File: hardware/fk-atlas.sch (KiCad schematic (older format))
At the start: 50 parts, among them J1 CONN-HDR-2x5, J2 MICRO-USB, J3 Conn_01x02, J4 Conn_01x07, Q1 2N7002LT1G, Q2 2N7002LT1G, Q3 2N7002LT1G, Q4 2N7002LT1G, Q5 2N7002LT1G, SW1 SPNO, U1 S25FL1xxK0XM, U2 ATSAMD21G18A-AU, U3 MCP1700T-3302E/MB, Y1 FC-135

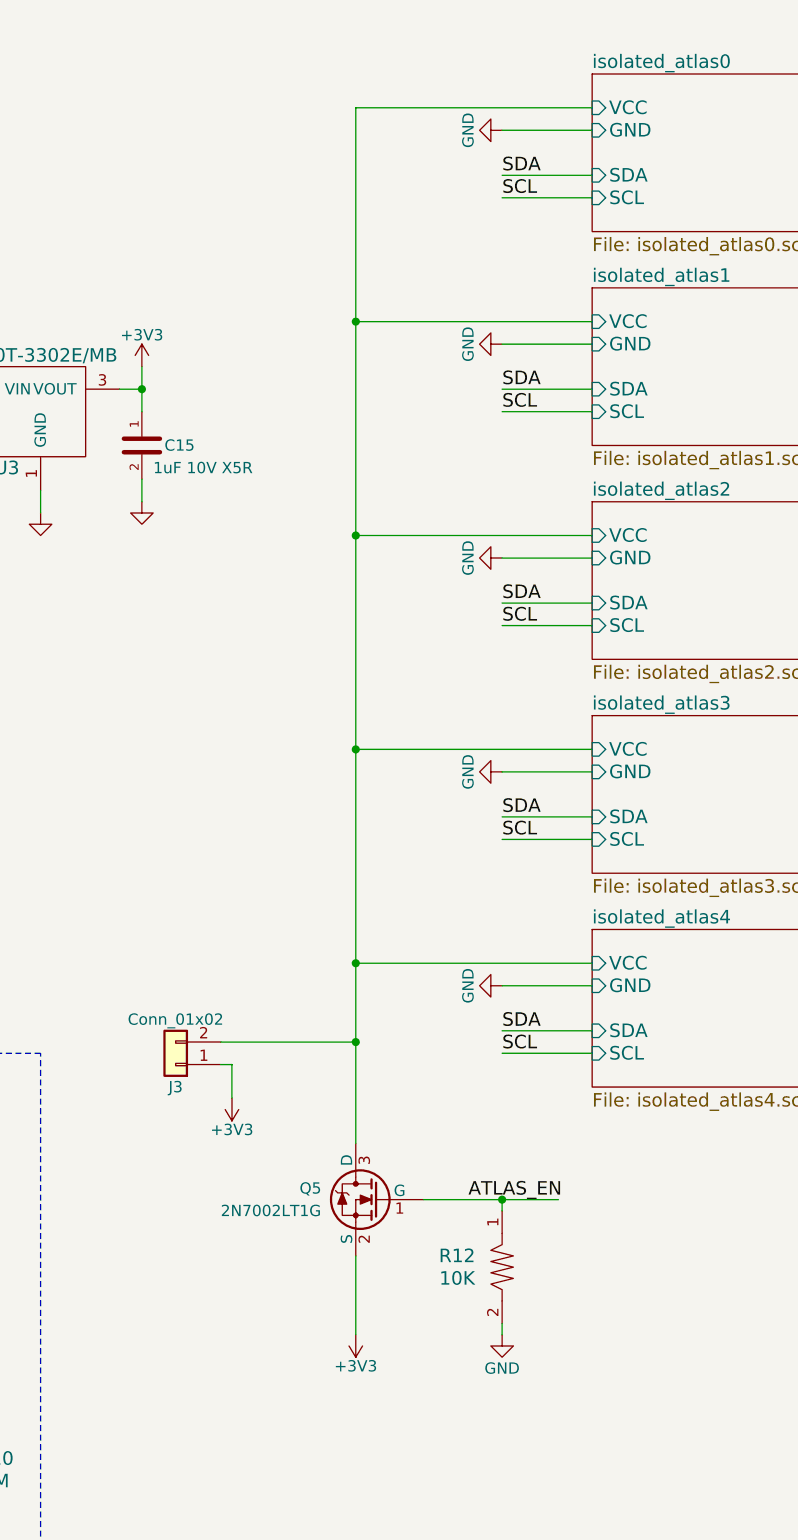
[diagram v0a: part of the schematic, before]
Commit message: Convert atlas enable to low side switch.
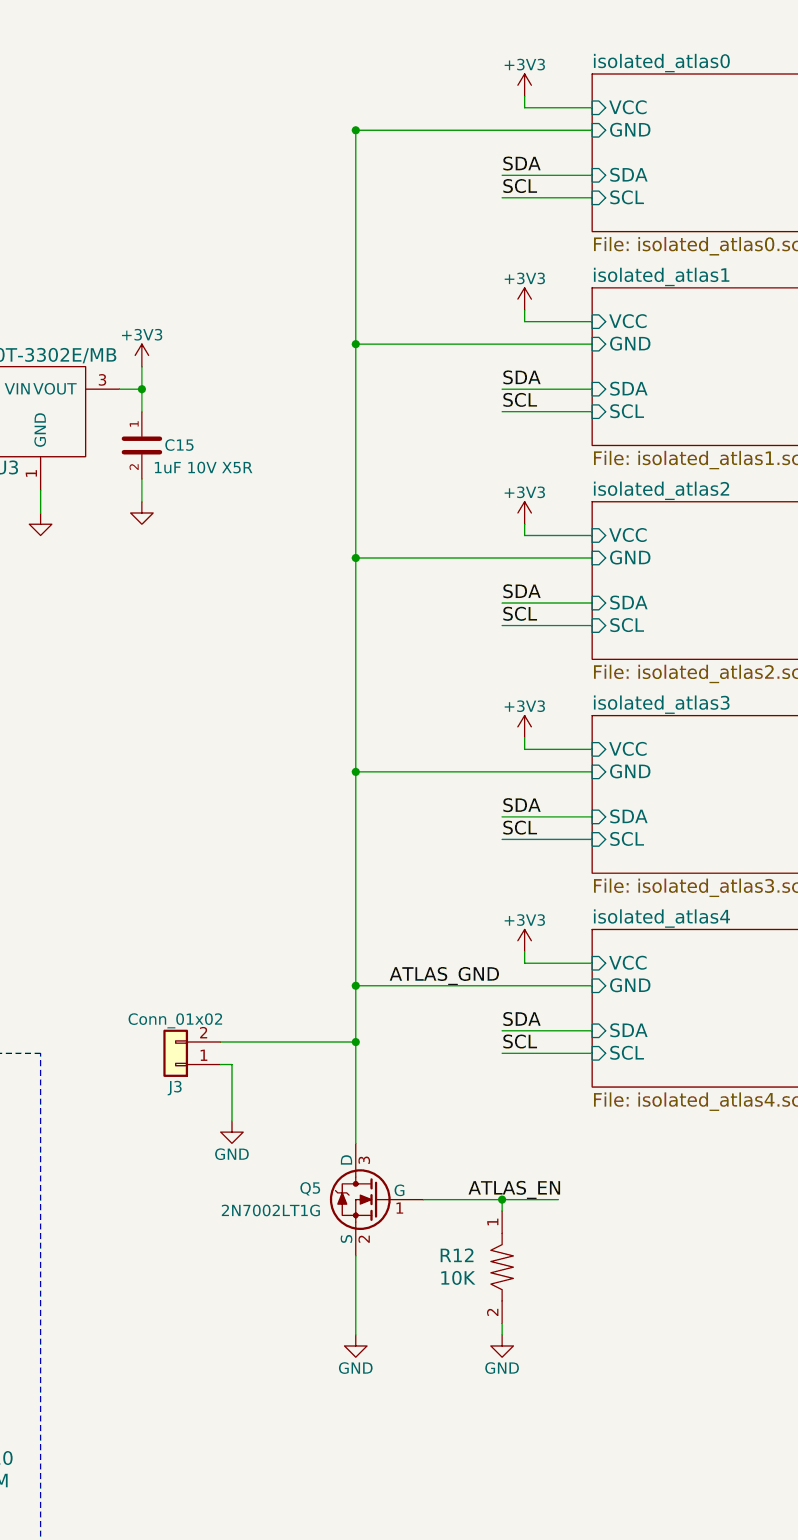
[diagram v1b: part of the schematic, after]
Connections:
- net labels added: ATLAS_GND
- wire segments 211 -> 216

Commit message: Break out Wire3 instead of Wire2.
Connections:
- net labels added: FLASH_CS, SCL1, SCL3, SDA1, SDA3
- net labels removed: D12, D3, D4, D5, SCL, SCL2, SDA, SDA2
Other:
- note removed: "RX1"
- note removed: "TX1"
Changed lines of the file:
@@
 	0    -1   -1   0
 $EndComp
-Text Label 2500 6800 0    60   ~ 0
-SCL
-Text Label 2500 6900 0    60   ~ 0
-SDA
-Text Label 4050 6050 0    60   ~ 0
-SDA
-Text Label 4050 5950 0    60   ~ 0
-SCL
+Text Label 2800 6800 0    50   ~ 0
+SCL1
+Text Label 2800 6900 0    50   ~ 0
+SDA1
+Text Label 4050 6050 0    50   ~ 0
+SDA1
+Text Label 4050 5950 0    50   ~ 0
+SCL1
 Text Label 13750 1400 0    60   ~ 0
-SCL
+SCL1
 Text Label 13750 1300 0    60   ~ 0
-SDA
+SDA1
 Text Label 13750 2350 0    60   ~ 0
-SCL
+SCL1
 Text Label 13750 2250 0    60   ~ 0
-SDA
+SDA1
 Text Label 13750 3300 0    60   ~ 0
-SCL
+SCL1
 Text Label 13750 3200 0    60   ~ 0
-SDA
+SDA1
 Text Label 13750 4250 0    60   ~ 0
-SCL
+SCL1
 Text Label 13750 4150 0    60   ~ 0
-SDA
+SDA1
 Text Label 13750 5200 0    60   ~ 0
-SCL
+SCL1
 Text Label 13750 5100 0    60   ~ 0
-SDA
+SDA1
 Text Label 2550 2300 0    50   ~ 0
 A0
@@
 Text Label 2550 2800 0    50   ~ 0
 D9
-Text Label 2550 2900 0    50   ~ 0
-D4
-Text Label 2550 3000 0    50   ~ 0
-D3
 Text Label 2550 3100 0    50   ~ 0
 D1
@@
 Text Label 2550 3500 0    50   ~ 0
 D2
-Text Label 2550 3600 0    50   ~ 0
-D5
 Text Label 2550 3700 0    50   ~ 0
 D11
 Text Label 2550 3900 0    50   ~ 0
 D10
-Text Label 2550 4000 0    50   ~ 0
-D12
 Text Label 2550 4100 0    50   ~ 0
 D6
@@
 D7
 Text Label 2550 4300 0    50   ~ 0
-SDA
+SDA1
 Text Label 2550 4400 0    50   ~ 0
-SCL
+SCL1
 Text Label 4550 3000 0    50   ~ 0
 MOSI
@@
 Text Notes 4850 2800 0    50   ~ 0
 RX0
-Text Notes 2350 3200 0    50   ~ 0
-RX1
-Text Notes 2350 3100 0    50   ~ 0
-TX1
 Text Notes 6000 4900 0    60   ~ 0
 1.27 mm (0.05")
@@
 D13
 Wire Wire Line
-	2400 6800 3200 6800
-Wire Wire Line
-	2400 6900 3500 6900
+	2800 6800 3200 6800
+Wire Wire Line
+	2800 6900 3500 6900
 Wire Wire Line
 	4350 5650 4100 5650
@@
 	2550 2800 2850 2800
 Wire Wire Line
-	2850 2900 2550 2900
-Wire Wire Line
-	2850 3000 2550 3000
+	2550 2900 2850 2900
+Wire Wire Line
+	2550 3000 2850 3000
 Wire Wire Line
 	2850 3100 2550 3100
@@
 	2850 3500 2550 3500
 Wire Wire Line
-	2850 3600 2550 3600
-Wire Wire Line
-	2000 3700 2850 3700
+	2400 3600 2850 3600
 Wire Wire Line
 	2550 3900 2850 3900
 Wire Wire Line
-	2000 4000 2850 4000
+	2400 4000 2850 4000
 Wire Wire Line
 	2850 4100 2550 4100
@@
 Wire Wire Line
 	11350 6650 11350 6750
-Wire Wire Line
-	2000 3800 2850 3800
 Wire Wire Line
 	5450 5900 5500 5900
@@
 Text Label 13600 5850 0    60   ~ 0
 ATLAS_EN
-Text Label 2000 4000 0    60   ~ 0
+Text Label 2400 4000 0    60   ~ 0
 ATLAS_EN
 Wire Wire Line
@@
 Wire Wire Line
 	12550 5250 12500 5250
-Text Label 2000 3700 0    50   ~ 0
-SDA2
-Text Label 2000 3800 0    50   ~ 0
-SCL2
+Text Label 2550 2900 0    50   ~ 0
+SDA3
+Text Label 2550 3000 0    50   ~ 0
+SCL3
 $Comp
 L Conn_01x07 J4
@@
 $EndComp
 Text Label 4050 6250 0    50   ~ 0
-SDA2
+SDA3
 Text Label 4050 6150 0    50   ~ 0
-SCL2
+SCL3
 Wire Wire Line
 	4050 6150 4350 6150
@@
 Text Label 3650 9650 0    60   ~ 0
 MOSI
-Text Label 2050 9450 0    60   ~ 0
+Text Label 1900 9450 0    60   ~ 0
 MISO
 $Comp
@@
 $EndComp
 Wire Wire Line
-	2050 9450 2350 9450
+	1900 9450 2350 9450
 Wire Wire Line
 	1850 9200 1850 9550
@@
 	1850 9550 2350 9550
 Wire Wire Line
-	2050 9350 2350 9350
-Text Label 2050 9350 0    50   ~ 0
-D5
+	1900 9350 2350 9350
+Text Label 1900 9350 0    50   ~ 0
+FLASH_CS
 $Comp
 L GND #PWR049
@@
 Text Label 13250 4900 0    60   ~ 0
 ATLAS_GND
+Wire Wire Line
+	2550 3700 2850 3700
+Wire Wire Line
+	2850 3800 2550 3800
+Text Label 2400 3600 0    50   ~ 0
+FLASH_CS
 $EndSCHEMATC

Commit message: Break out D30/D31 serial lines.
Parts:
- removed J4: Conn_01x07, Socket_Strips:Socket_Strip_Straight_1x07_Pitch2.54mm, symbol Conn_01x07
- added J4: Conn_01x09, Socket_Strips:Socket_Strip_Straight_1x09_Pitch2.54mm, symbol Conn_01x09
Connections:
- wire segments 216 -> 218
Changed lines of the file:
@@
 Text Label 2550 3000 0    50   ~ 0
 SCL3
-$Comp
-L Conn_01x07 J4
-U 1 1 5A0F83DC
-P 4550 5950
-F 0 "J4" H 4550 6350 50  0000 C CNN
-F 1 "Conn_01x07" H 4550 5550 50  0000 C CNN
-F 2 "Socket_Strips:Socket_Strip_Straight_1x07_Pitch2.54mm" H 4550 5950 50  0001 C CNN
-F 3 "" H 4550 5950 50  0001 C CNN
-	1    4550 5950
-	1    0    0    -1
-$EndComp
 Text Label 4050 6250 0    50   ~ 0
 SDA3
@@
 Text Label 2400 3600 0    50   ~ 0
 FLASH_CS
+$Comp
+L Conn_01x09 J4
+U 1 1 5A46F380
+P 4550 6050
+F 0 "J4" H 4550 6550 50  0000 C CNN
+F 1 "Conn_01x09" H 4550 5550 50  0000 C CNN
+F 2 "Socket_Strips:Socket_Strip_Straight_1x09_Pitch2.54mm" H 4550 6050 50  0001 C CNN
+F 3 "" H 4550 6050 50  0001 C CNN
+	1    4550 6050
+	1    0    0    -1
+$EndComp
+Wire Wire Line
+	4050 6350 4350 6350
+Wire Wire Line
+	4050 6450 4350 6450
+Text Label 4050 6450 0    50   ~ 0
+D31
+Text Label 4050 6350 0    50   ~ 0
+D30
 $EndSCHEMATC
